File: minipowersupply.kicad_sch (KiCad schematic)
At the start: 0 parts

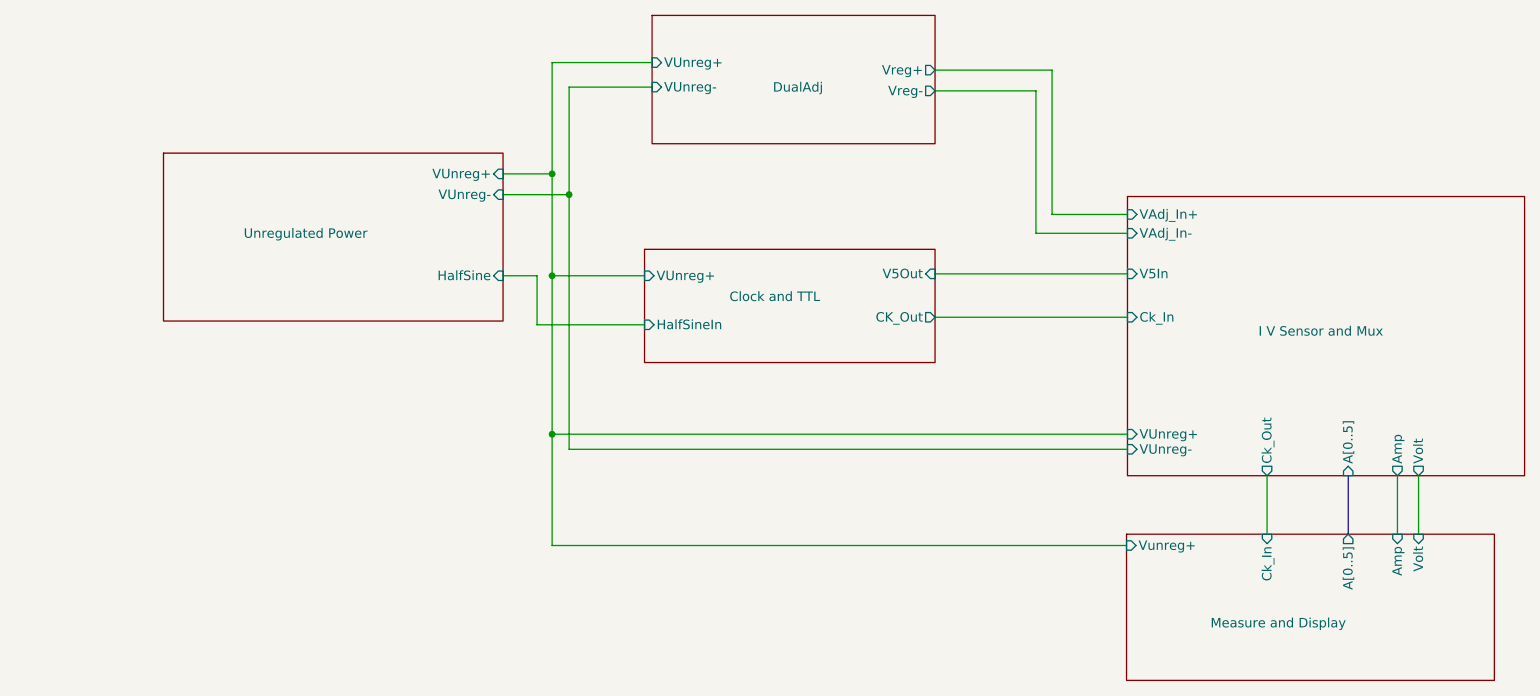
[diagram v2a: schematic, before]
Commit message: adding diff and summing amps to scale amp inputs
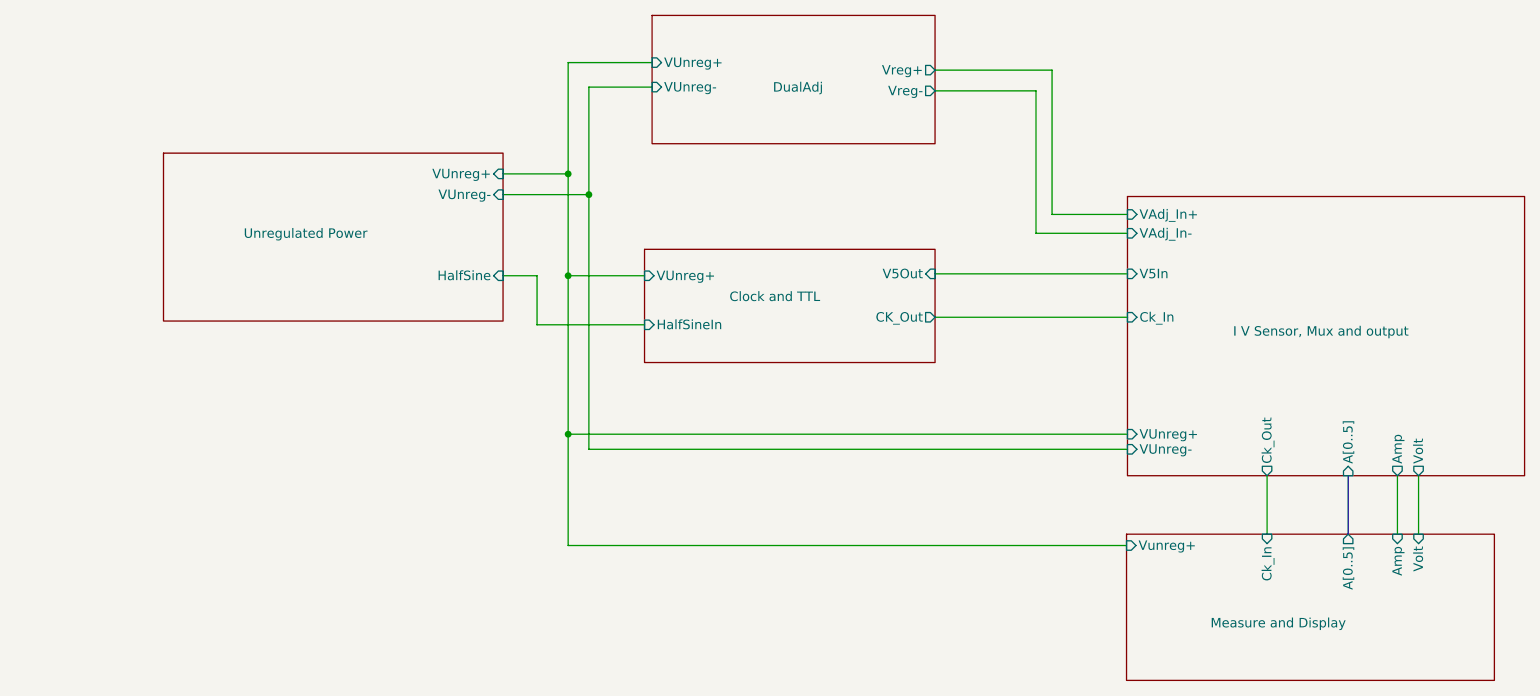
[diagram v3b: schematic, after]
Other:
- sheet I V Sensor and Mux renamed I V Sensor, Mux and output
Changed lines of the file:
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@@
     (company "Beyond Lame")
   )
-  (junction (at 106.045 87.884) (diameter 0) (color 0 0 0 0)
-  )
-  (junction (at 108.331 76.962) (diameter 0) (color 0 0 0 0)
-  )
-  (junction (at 106.045 109.22) (diameter 0) (color 0 0 0 0)
-  )
-  (junction (at 106.045 74.168) (diameter 0) (color 0 0 0 0)
+  (junction (at 110.998 76.962) (diameter 0) (color 0 0 0 0)
+  )
+  (junction (at 108.204 109.22) (diameter 0) (color 0 0 0 0)
+  )
+  (junction (at 108.204 74.168) (diameter 0) (color 0 0 0 0)
+  )
+  (junction (at 108.204 87.884) (diameter 0) (color 0 0 0 0)
   )
   (wire (pts (xy 157.607 87.63) (xy 183.515 87.63))
@@
     (stroke (width 0) (type default) (color 0 0 0 0))
   )
-  (wire (pts (xy 99.441 76.962) (xy 108.331 76.962))
+  (wire (pts (xy 99.441 76.962) (xy 110.998 76.962))
     (stroke (width 0) (type default) (color 0 0 0 0))
   )
@@
     (stroke (width 0) (type default) (color 0 0 0 0))
   )
-  (wire (pts (xy 106.045 109.22) (xy 106.045 124.206))
-    (stroke (width 0) (type default) (color 0 0 0 0))
-  )
-  (wire (pts (xy 108.331 111.252) (xy 183.515 111.252))
+  (wire (pts (xy 108.204 87.884) (xy 108.204 109.22))
+    (stroke (width 0) (type default) (color 0 0 0 0))
+  )
+  (wire (pts (xy 110.998 111.252) (xy 183.515 111.252))
     (stroke (width 0) (type default) (color 0 0 0 0))
   )
@@
     (stroke (width 0) (type default) (color 0 0 0 0))
   )
-  (wire (pts (xy 183.388 124.206) (xy 106.045 124.206))
+  (wire (pts (xy 183.388 124.206) (xy 108.204 124.206))
     (stroke (width 0) (type default) (color 0 0 0 0))
   )
@@
     (stroke (width 0) (type default) (color 0 0 0 0))
   )
-  (wire (pts (xy 106.045 87.884) (xy 106.045 109.22))
-    (stroke (width 0) (type default) (color 0 0 0 0))
-  )
   (wire (pts (xy 171.196 62.992) (xy 157.607 62.992))
     (stroke (width 0) (type default) (color 0 0 0 0))
@@
     (stroke (width 0) (type default) (color 0 0 0 0))
   )
-  (wire (pts (xy 106.045 87.884) (xy 118.491 87.884))
-    (stroke (width 0) (type default) (color 0 0 0 0))
-  )
-  (wire (pts (xy 106.045 74.168) (xy 106.045 87.884))
-    (stroke (width 0) (type default) (color 0 0 0 0))
-  )
-  (wire (pts (xy 108.331 76.962) (xy 108.331 111.252))
+  (wire (pts (xy 108.204 87.884) (xy 118.491 87.884))
+    (stroke (width 0) (type default) (color 0 0 0 0))
+  )
+  (wire (pts (xy 108.204 59.182) (xy 108.204 74.168))
+    (stroke (width 0) (type default) (color 0 0 0 0))
+  )
+  (wire (pts (xy 110.998 76.962) (xy 110.998 111.252))
     (stroke (width 0) (type default) (color 0 0 0 0))
   )
@@
     (stroke (width 0) (type default) (color 0 0 0 0))
   )
-  (wire (pts (xy 108.331 62.484) (xy 108.331 76.962))
-    (stroke (width 0) (type default) (color 0 0 0 0))
-  )
-  (wire (pts (xy 183.515 109.22) (xy 106.045 109.22))
+  (wire (pts (xy 110.998 62.484) (xy 110.998 76.962))
+    (stroke (width 0) (type default) (color 0 0 0 0))
+  )
+  (wire (pts (xy 108.204 109.22) (xy 183.515 109.22))
     (stroke (width 0) (type default) (color 0 0 0 0))
   )
@@
     (stroke (width 0) (type default) (color 0 0 0 0))
   )
-  (wire (pts (xy 106.045 59.182) (xy 106.045 74.168))
-    (stroke (width 0) (type default) (color 0 0 0 0))
-  )
   (wire (pts (xy 173.355 79.629) (xy 183.515 79.629))
     (stroke (width 0) (type default) (color 0 0 0 0))
   )
-  (wire (pts (xy 119.507 59.182) (xy 106.045 59.182))
-    (stroke (width 0) (type default) (color 0 0 0 0))
-  )
-  (wire (pts (xy 99.441 74.168) (xy 106.045 74.168))
-    (stroke (width 0) (type default) (color 0 0 0 0))
-  )
-  (wire (pts (xy 119.507 62.484) (xy 108.331 62.484))
+  (wire (pts (xy 119.507 59.182) (xy 108.204 59.182))
+    (stroke (width 0) (type default) (color 0 0 0 0))
+  )
+  (wire (pts (xy 99.441 74.168) (xy 108.204 74.168))
+    (stroke (width 0) (type default) (color 0 0 0 0))
+  )
+  (wire (pts (xy 108.204 74.168) (xy 108.204 87.884))
+    (stroke (width 0) (type default) (color 0 0 0 0))
+  )
+  (wire (pts (xy 119.507 62.484) (xy 110.998 62.484))
+    (stroke (width 0) (type default) (color 0 0 0 0))
+  )
+  (wire (pts (xy 108.204 109.22) (xy 108.204 124.206))
     (stroke (width 0) (type default) (color 0 0 0 0))
   )
@@
     (stroke (width 0.1524) (type solid) (color 0 0 0 0))
     (fill (color 0 0 0 0.0000))
-    (property "Sheet name" "I V Sensor and Mux" (id 0) (at 209.55 94.615 0)
+    (property "Sheet name" "I V Sensor, Mux and output" (id 0) (at 209.55 94.615 0)
       (effects (font (size 1.27 1.27)) (justify top))
     )
@@
       (reference "#PWR031") (unit 1) (value "GNDREF") (footprint "")
     )
+    (path "/e84becbb-d7bb-4f82-b4d3-8ddac9da005f/e4676b07-9834-40db-b874-f1b94add0c26"
+      (reference "#PWR032") (unit 1) (value "GNDREF") (footprint "")
+    )
     (path "/f603f830-1954-4cf1-9214-ed1b9cc75116/9e49a0e5-227d-4a50-a1e1-04e81c4e4cef/4496cfa9-1f5e-49b8-b439-1895b1d3b362"
       (reference "#PWR033") (unit 1) (value "GNDREF") (footprint "")
@@
       (reference "#PWR034") (unit 1) (value "GNDREF") (footprint "")
     )
+    (path "/e84becbb-d7bb-4f82-b4d3-8ddac9da005f/345e8c4c-c72f-421a-87e5-a0e31bba22a8"
+      (reference "#PWR035") (unit 1) (value "GNDREF") (footprint "")
+    )
     (path "/f603f830-1954-4cf1-9214-ed1b9cc75116/b0d622a9-3316-43e0-a924-cdea4dccff2a/4496cfa9-1f5e-49b8-b439-1895b1d3b362"
       (reference "#PWR036") (unit 1) (value "GNDREF") (footprint "")
@@
       (reference "#PWR0103") (unit 1) (value "GNDREF") (footprint "")
     )
+    (path "/e84becbb-d7bb-4f82-b4d3-8ddac9da005f/f06859c6-a77e-4185-a978-826707d85879"
+      (reference "#PWR0104") (unit 1) (value "GNDREF") (footprint "")
+    )
+    (path "/e84becbb-d7bb-4f82-b4d3-8ddac9da005f/348e0afa-04d3-4f28-bd59-b9a93f41a2a5"
+      (reference "#PWR0105") (unit 1) (value "GNDREF") (footprint "")
+    )
     (path "/e84becbb-d7bb-4f82-b4d3-8ddac9da005f/e18d8df6-911d-4892-87af-96bc187d73d0"
       (reference "A1") (unit 1) (value "Arduino_Nano_v3.x") (footprint "Module:Arduino_Nano")
@@
       (reference "R26") (unit 1) (value "10k") (footprint "Resistor_SMD:R_0603_1608Metric")
     )
+    (path "/e84becbb-d7bb-4f82-b4d3-8ddac9da005f/c1a1158e-97cc-4067-ab7b-aaf59d9d2592"
+      (reference "R27") (unit 1) (value "100k") (footprint "Resistor_SMD:R_0603_1608Metric")
+    )
+    (path "/e84becbb-d7bb-4f82-b4d3-8ddac9da005f/78108de0-023e-4397-90e8-0476f4747fae"
+      (reference "R28") (unit 1) (value "10k") (footprint "Resistor_SMD:R_0603_1608Metric")
+    )
+    (path "/e84becbb-d7bb-4f82-b4d3-8ddac9da005f/a4e3fd44-9c95-4684-8069-253d39e01fef"
+      (reference "R29") (unit 1) (value "10k") (footprint "Resistor_SMD:R_0603_1608Metric")
+    )
+    (path "/e84becbb-d7bb-4f82-b4d3-8ddac9da005f/55a74c9c-0472-4cf8-90c5-b5bad3b999e3"
+      (reference "R30") (unit 1) (value "10k") (footprint "Resistor_SMD:R_0603_1608Metric")
+    )
+    (path "/e84becbb-d7bb-4f82-b4d3-8ddac9da005f/62bb0dec-d209-435d-adeb-9002fe77de49"
+      (reference "R31") (unit 1) (value "10k") (footprint "Resistor_SMD:R_0603_1608Metric")
+    )
+    (path "/e84becbb-d7bb-4f82-b4d3-8ddac9da005f/428e6b73-f17f-425f-adb5-884c4161e622"
+      (reference "R32") (unit 1) (value "100k") (footprint "Resistor_SMD:R_0603_1608Metric")
+    )
     (path "/ad7d34fc-ea53-4304-ba5f-b50b36043af6/ffb63565-cbf3-4724-bc54-d6a7b5aa1900"
       (reference "RV1") (unit 1) (value "5k") (footprint "")
@@
     )
     (path "/e84becbb-d7bb-4f82-b4d3-8ddac9da005f/23311901-7468-4bf4-aafc-bbb1c10a97fd"
-      (reference "SW1") (unit 1) (value "RotaryEncoder_Switch") (footprint "Rotary_Encoder:RotaryEncoder_Alps_EC11E_Vertical_H20mm")
+      (reference "SW1") (unit 1) (value "RotaryEncoder_Switch") (footprint "Rotary_Encoder:RotaryEncoder_Alps_EC11E-Switch_Vertical_H20mm_CircularMountingHoles")
     )
     (path "/0171d92e-8d18-4439-a831-c9696203c470/6f0fe44a-f55d-46f7-974a-ed9861cce930"
@@
       (reference "U11") (unit 1) (value "74HC4051") (footprint "Package_SO:TSSOP-16_4.4x5mm_P0.65mm")
     )
-  )
+    (path "/e84becbb-d7bb-4f82-b4d3-8ddac9da005f/c1421d5d-6659-42ae-b879-0c0b448023ee"
+      (reference "U12") (unit 1) (value "LM358_DFN") (footprint "Package_DFN_QFN:DFN-8-1EP_2x2mm_P0.5mm_EP1.05x1.75mm")
+    )
+    (path "/e84becbb-d7bb-4f82-b4d3-8ddac9da005f/e3f8995c-5e56-41ed-8713-ecf75f6b8936"
+      (reference "U12") (unit 2) (value "LM358_DFN") (footprint "Package_DFN_QFN:DFN-8-1EP_2x2mm_P0.5mm_EP1.05x1.75mm")
+    )
+    (path "/e84becbb-d7bb-4f82-b4d3-8ddac9da005f/7af98bce-8b4c-4833-a1c6-bcd588f589c7"
+      (reference "U12") (unit 3) (value "LM358_DFN") (footprint "Package_DFN_QFN:DFN-8-1EP_2x2mm_P0.5mm_EP1.05x1.75mm")
+    )
+  )

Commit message: added new op amps and used automated traces due to complexity
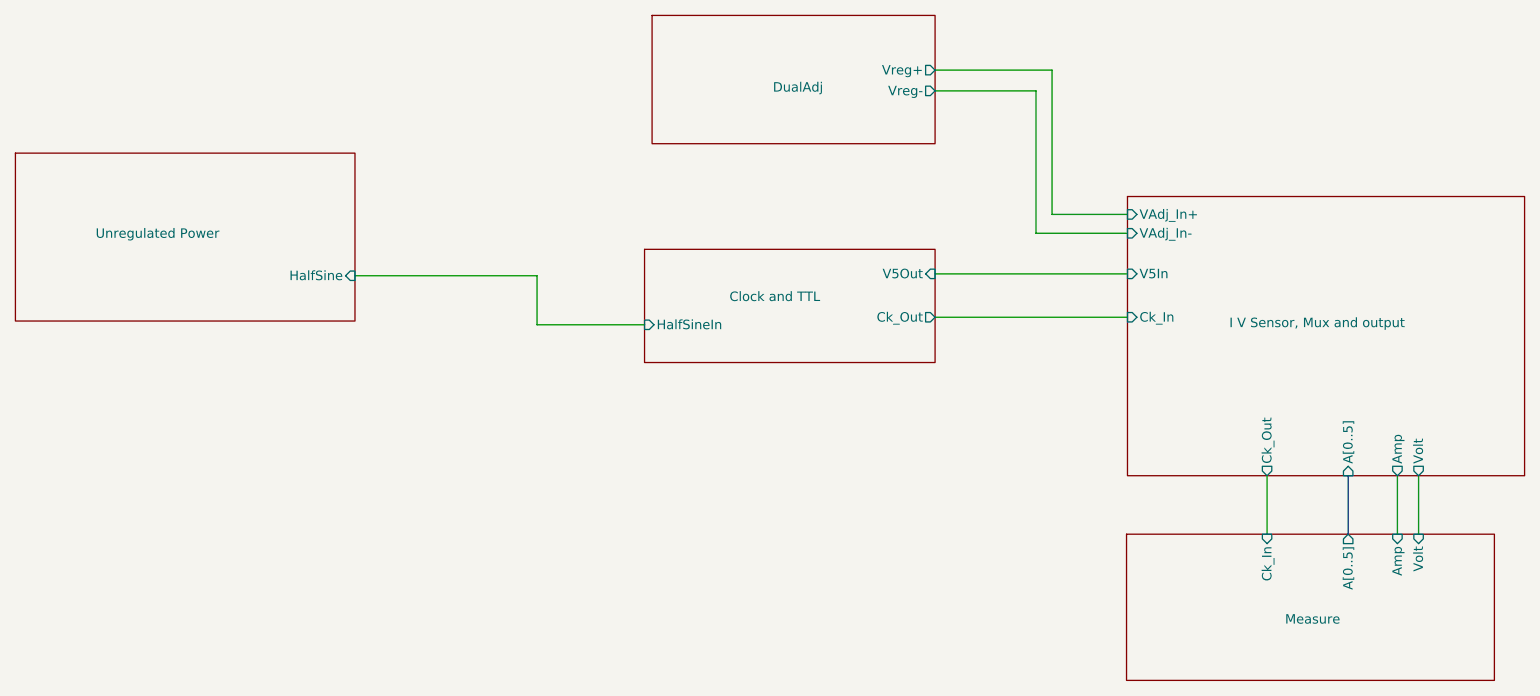
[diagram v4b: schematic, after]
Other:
- sheet Measure and Display renamed Measure
- sheet Clock and TTL ports: added Ck_Out; removed CK_Out, VUnreg+
- sheet DualAdj ports: added none; removed VUnreg+, VUnreg-
- sheet I V Sensor, Mux and output ports: added none; removed VUnreg+, VUnreg-
- sheet Measure ports: added none; removed Vunreg+
- sheet Unregulated Power ports: added none; removed VUnreg+, VUnreg-

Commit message: working on MUX and pre-amp layout
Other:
- sheet I V Sensor, Mux and output ports: added none; removed Ck_Out
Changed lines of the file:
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@@
       (effects (font (size 1.27 1.27)) (justify left))
     )
-    (pin "Ck_Out" output (at 202.311 114.808 270)
+    (pin "Ck_In" output (at 202.311 114.808 270)
       (effects (font (size 1.27 1.27)) (justify left))
     )
@@
   )
   (symbol_instances
+    (path "/e84becbb-d7bb-4f82-b4d3-8ddac9da005f/621ef44c-3296-4351-8096-bd595137f560"
+      (reference "#FLG01") (unit 1) (value "PWR_FLAG") (footprint "")
+    )
+    (path "/e84becbb-d7bb-4f82-b4d3-8ddac9da005f/d6f1f591-bd83-42e0-8e8f-8d7ab69527bc"
+      (reference "#FLG02") (unit 1) (value "PWR_FLAG") (footprint "")
+    )
     (path "/0171d92e-8d18-4439-a831-c9696203c470/901b8763-0514-4c6a-ba23-6ed863683be5"
       (reference "#FLG0101") (unit 1) (value "PWR_FLAG") (footprint "")
@@
       (reference "#FLG0102") (unit 1) (value "PWR_FLAG") (footprint "")
     )
+    (path "/e84becbb-d7bb-4f82-b4d3-8ddac9da005f/e3fa7d7a-3848-4890-b265-815c8a233db0"
+      (reference "#FLG0103") (unit 1) (value "PWR_FLAG") (footprint "")
+    )
+    (path "/f603f830-1954-4cf1-9214-ed1b9cc75116/4a2ef75f-a9f8-44de-951c-5cf27de4596e/9c7f1c7f-d1e0-4615-9d54-bf6cc10023f0"
+      (reference "#FLG0104") (unit 1) (value "PWR_FLAG") (footprint "")
+    )
+    (path "/f603f830-1954-4cf1-9214-ed1b9cc75116/b8bbf3ce-a44d-42ed-83f6-0adf6f7aba5f/9c7f1c7f-d1e0-4615-9d54-bf6cc10023f0"
+      (reference "#FLG0105") (unit 1) (value "PWR_FLAG") (footprint "")
+    )
+    (path "/f603f830-1954-4cf1-9214-ed1b9cc75116/5ce8b93a-cbca-477e-a92d-146187ab8a69/9c7f1c7f-d1e0-4615-9d54-bf6cc10023f0"
+      (reference "#FLG0106") (unit 1) (value "PWR_FLAG") (footprint "")
+    )
+    (path "/f603f830-1954-4cf1-9214-ed1b9cc75116/9e49a0e5-227d-4a50-a1e1-04e81c4e4cef/9c7f1c7f-d1e0-4615-9d54-bf6cc10023f0"
+      (reference "#FLG0107") (unit 1) (value "PWR_FLAG") (footprint "")
+    )
+    (path "/f603f830-1954-4cf1-9214-ed1b9cc75116/b0d622a9-3316-43e0-a924-cdea4dccff2a/9c7f1c7f-d1e0-4615-9d54-bf6cc10023f0"
+      (reference "#FLG0108") (unit 1) (value "PWR_FLAG") (footprint "")
+    )
+    (path "/f603f830-1954-4cf1-9214-ed1b9cc75116/e4ade9a2-b9aa-4eb4-a543-5aaded3890ac"
+      (reference "#FLG0109") (unit 1) (value "PWR_FLAG") (footprint "")
+    )
+    (path "/f603f830-1954-4cf1-9214-ed1b9cc75116/3dd88c08-a199-4df4-bc03-2f7fe30549bb"
+      (reference "#FLG0110") (unit 1) (value "PWR_FLAG") (footprint "")
+    )
+    (path "/f603f830-1954-4cf1-9214-ed1b9cc75116/336c7a9b-a31d-4694-996b-4c8d256b1679"
+      (reference "#FLG0111") (unit 1) (value "PWR_FLAG") (footprint "")
+    )
+    (path "/04da8333-1ee2-480f-9c82-cd475e7d9e9d/fd4adc55-ee15-4112-8fdb-a7ad1c8ae125"
+      (reference "#FLG0112") (unit 1) (value "PWR_FLAG") (footprint "")
+    )
+    (path "/ad7d34fc-ea53-4304-ba5f-b50b36043af6/965b1e40-4885-4f54-98b2-5b0b9b5e2914"
+      (reference "#FLG0113") (unit 1) (value "PWR_FLAG") (footprint "")
+    )
+    (path "/ad7d34fc-ea53-4304-ba5f-b50b36043af6/766a0ed4-74e9-4ae4-bb27-c65729b84214"
+      (reference "#FLG0114") (unit 1) (value "PWR_FLAG") (footprint "")
+    )
+    (path "/f603f830-1954-4cf1-9214-ed1b9cc75116/4a2ef75f-a9f8-44de-951c-5cf27de4596e/d84c0cb6-4bc6-4869-9ec5-2f79b76866ed"
+      (reference "#FLG0115") (unit 1) (value "PWR_FLAG") (footprint "")
+    )
+    (path "/f603f830-1954-4cf1-9214-ed1b9cc75116/b8bbf3ce-a44d-42ed-83f6-0adf6f7aba5f/d84c0cb6-4bc6-4869-9ec5-2f79b76866ed"
+      (reference "#FLG0116") (unit 1) (value "PWR_FLAG") (footprint "")
+    )
+    (path "/f603f830-1954-4cf1-9214-ed1b9cc75116/5ce8b93a-cbca-477e-a92d-146187ab8a69/d84c0cb6-4bc6-4869-9ec5-2f79b76866ed"
+      (reference "#FLG0117") (unit 1) (value "PWR_FLAG") (footprint "")
+    )
+    (path "/f603f830-1954-4cf1-9214-ed1b9cc75116/9e49a0e5-227d-4a50-a1e1-04e81c4e4cef/d84c0cb6-4bc6-4869-9ec5-2f79b76866ed"
+      (reference "#FLG0118") (unit 1) (value "PWR_FLAG") (footprint "")
+    )
+    (path "/f603f830-1954-4cf1-9214-ed1b9cc75116/b0d622a9-3316-43e0-a924-cdea4dccff2a/d84c0cb6-4bc6-4869-9ec5-2f79b76866ed"
+      (reference "#FLG0119") (unit 1) (value "PWR_FLAG") (footprint "")
+    )
     (path "/f603f830-1954-4cf1-9214-ed1b9cc75116/4a2ef75f-a9f8-44de-951c-5cf27de4596e/4496cfa9-1f5e-49b8-b439-1895b1d3b362"
       (reference "#PWR01") (unit 1) (value "GNDREF") (footprint "")
@@
       (reference "#PWR038") (unit 1) (value "GNDREF") (footprint "")
     )
+    (path "/e84becbb-d7bb-4f82-b4d3-8ddac9da005f/267148e3-6a4d-4787-853e-d97a2f4d8c72"
+      (reference "#PWR039") (unit 1) (value "GNDREF") (footprint "")
+    )
     (path "/f603f830-1954-4cf1-9214-ed1b9cc75116/7c26e0c0-ea2d-4523-96ca-f37c5df5f7f2"
       (reference "#PWR0101") (unit 1) (value "GNDREF") (footprint "")
@@
       (reference "C36") (unit 1) (value "0.1uF") (footprint "Capacitor_SMD:C_0603_1608Metric")
     )
+    (path "/e84becbb-d7bb-4f82-b4d3-8ddac9da005f/89e8357c-2988-4c84-a336-7eefb7ad8303"
+      (reference "C37") (unit 1) (value "0.1uF") (footprint "Capacitor_SMD:C_0603_1608Metric")
+    )
     (path "/f603f830-1954-4cf1-9214-ed1b9cc75116/4c3c0772-d8ab-4f0d-a763-9db1013777da"
       (reference "C38") (unit 1) (value "0.1uF") (footprint "Capacitor_SMD:C_0603_1608Metric")
@@
       (reference "U12") (unit 1) (value "LM358") (footprint "Package_SO:TSSOP-8_4.4x3mm_P0.65mm")
     )
-    (path "/e84becbb-d7bb-4f82-b4d3-8ddac9da005f/c1421d5d-6659-42ae-b879-0c0b448023ee"
+    (path "/e84becbb-d7bb-4f82-b4d3-8ddac9da005f/c2acf3d5-e5ed-4c68-b47c-eedda8a9a209"
       (reference "U12") (unit 2) (value "LM358") (footprint "Package_SO:TSSOP-8_4.4x3mm_P0.65mm")
     )
@@
       (reference "U13") (unit 1) (value "LM358") (footprint "Package_SO:TSSOP-8_4.4x3mm_P0.65mm")
     )
-    (path "/e84becbb-d7bb-4f82-b4d3-8ddac9da005f/c2acf3d5-e5ed-4c68-b47c-eedda8a9a209"
+    (path "/e84becbb-d7bb-4f82-b4d3-8ddac9da005f/c1421d5d-6659-42ae-b879-0c0b448023ee"
       (reference "U13") (unit 2) (value "LM358") (footprint "Package_SO:TSSOP-8_4.4x3mm_P0.65mm")
     )
